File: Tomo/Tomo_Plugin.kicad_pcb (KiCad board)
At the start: 2 copper layers, 35.6 x 55.9 mm, 26 parts, among them J002 STANDOFF_GND, J101 Raspberry_Pi_1, J102 CONN_01X02, J301 CONN_02X03, J401 CONN_01X04, J501 CONN_01X04, J502 CONN_01X03, J503 CONN_01X04, J601 CONN_01X04, U001 Designed_With_Kicad, U002 KwanSystems, U301 ADuM3221, U401 Arduino_Nano, U501 MPU9250

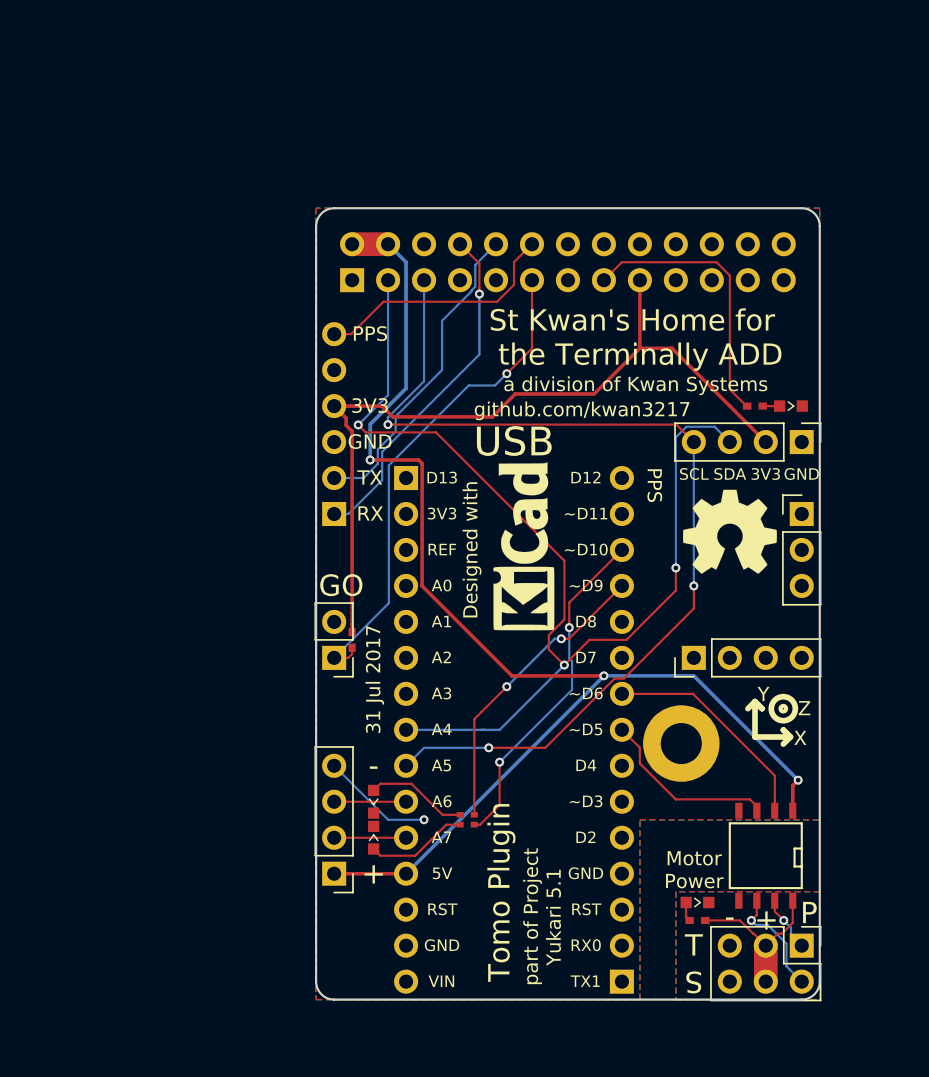
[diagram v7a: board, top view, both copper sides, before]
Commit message: Rework to solve solder mask problem and use 1206 parts
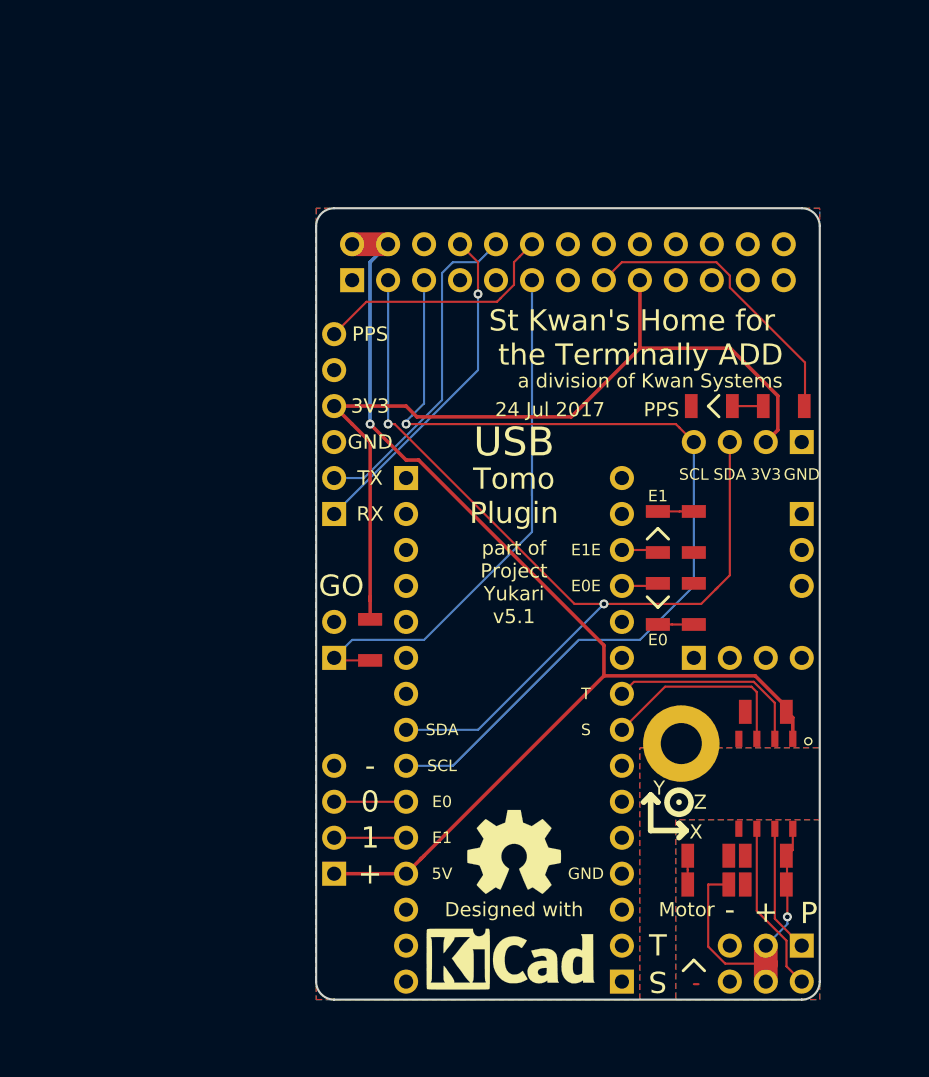
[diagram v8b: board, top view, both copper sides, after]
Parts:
- removed D115, D432: RED, KwanSystems:D_0603
- removed D306: GREEN, KwanSystems:D_0603
- removed D417: YELLOW, KwanSystems:D_0603
- removed R115, R306: 1.5k, KwanSystems:SMD_0402
- removed R122: RP2, KwanSystems:R_Array_Convex_2x0402
- removed REF**: KiCAD Logo, KwanSystems:Symbol_KiCAD-Logo_CopperAndSilkScreenTop_small
- added C301: 100nF, KwanSystems:SMD_1206, F.Cu at (158.2, 134.2)
- added C305: 100nF, KwanSystems:SMD_1206, F.Cu at (158.2, 144.3)
- added C308: 10uF, KwanSystems:SMD_1206, F.Cu at (158.2, 146.4)
- added D112: RED, KwanSystems:D_1206, F.Cu at (154.4, 112.6)
- added D308: BLUE, KwanSystems:D_1206, F.Cu at (154.2, 146.4)
- added D409: GREEN, KwanSystems:D_1206, F.Cu at (150.6, 126.6)
- added D410: YELLOW, KwanSystems:D_1206, F.Cu at (150.6, 121.5)
- added R112: 220, KwanSystems:SMD_1206, F.Cu at (159.5, 112.6)
- added R308: 220, KwanSystems:SMD_1206, F.Cu at (154.2, 144.3)
- added R409: 220, KwanSystems:SMD_1206, F.Cu at (153.2, 126.6)
- added R410: 220, KwanSystems:SMD_1206, F.Cu at (153.2, 121.5)
- R117: footprint KwanSystems:SMD_0402 -> KwanSystems:SMD_1206
- moved U001 29.0 mm to (140.2, 151.5), turned to 0 degrees
- moved REF*** 27.3 mm to (140.5, 144.1)
- moved G*** 19.8 mm to (157.0, 109.3), turned to 180 degrees
- moved REF*** 19.7 mm to (157.0, 145.6), turned to 180 degrees
- moved U501 9.89 mm to (150.1, 142.6)
- moved U301 5.08 mm to (158.2, 139.3)
- moved R117 1.27 mm to (130.3, 129.1)
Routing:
- net /E1_ECHO: track 24.1 -> 2.55 mm, vias 2 -> 0
- net /E0_ECHO: track 21.1 -> 2.55 mm, vias 2 -> 0
- net +BATT: track 11.7 -> 22.4 mm, vias 0 -> 1
- net +5V: track 91.2 -> 82.1 mm, vias 3 -> 1
- net /SDA: track 76.6 -> 67.7 mm, vias 3 -> 2
- net GND: track 7.93 -> 0.00 mm, vias 1 -> 0
- net /E1_ECHO+: track 7.21 -> 0.00 mm
- net /E0_ECHO+: track 7.21 -> 0.00 mm
- net /THROTTLE_HI: track 3.96 -> 10.1 mm, vias 1 -> 0
- net /STEER_HI: track 7.83 -> 12.1 mm, vias 1 -> 0
- net /GO_BTN: track 36.5 -> 40.6 mm, vias 1 -> 0
- net +3V3: track 56.8 -> 59.8 mm
- net /SCL: track 70.1 -> 67.3 mm, vias 3 -> 1
- net /E1_ECHO-: track 0.00 -> 2.54 mm
- net /E0_ECHO-: track 0.00 -> 2.54 mm
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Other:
- net class 3.3VPower added: clearance 0.1524, trace_width 0.254, via_dia 0.635, via_drill 0.3302
- net class BattPower added: clearance 0.1524, trace_width 0.1524, via_dia 0.635, via_drill 0.3302
- board text added: "0"
- board text added: "1"
- board text added: "24 Jul 2017"
- board text added: "E0"
- board text added: "E1"
- board text added: "Motor"
- board text added: "part of Project Yukari v5.1"
- board text removed: "31 Jul 2017"
- board text removed: "Motor Power"
- board text removed: "github.com/kwan3217"
- board text removed: "part of Project Yukari 5.1"
